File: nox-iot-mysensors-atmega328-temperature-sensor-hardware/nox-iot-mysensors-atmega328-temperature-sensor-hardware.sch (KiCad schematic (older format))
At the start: 14 parts, among them J1 Vin, J2 FTDI232, J3 AHT10, J4 TP4056, J5 Switch Connector, U1 ATmega328P-PU, U2 WAVGAT 3.3V, U3 NRF24L01+, Y1 16 MHZ

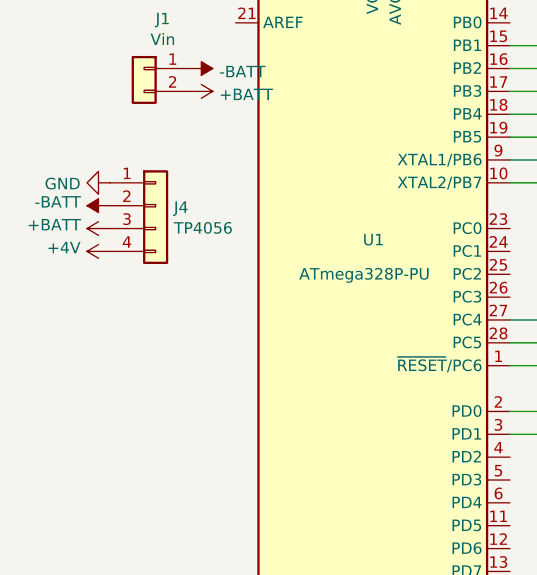
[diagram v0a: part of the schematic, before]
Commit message: updated with proper pcb
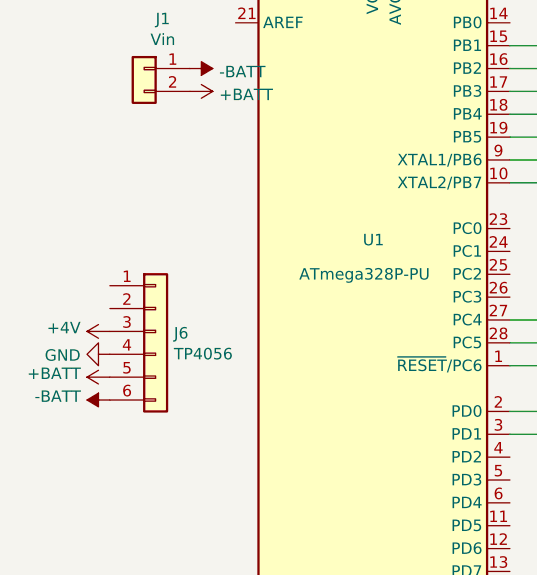
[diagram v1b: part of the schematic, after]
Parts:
- removed J4: TP4056, Connector_PinSocket_2.54mm:PinSocket_1x04_P2.54mm_Vertical, symbol Connector_Generic:Conn_01x04
- added J6: TP4056, Custom_Misc_Footprints:TP4056, symbol Connector_Generic:Conn_01x06
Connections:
- net +4V: now also J6.3 (Pin_3)
- net +BATT: now also J6.5 (Pin_5)
- net -BATT: now also J6.6 (Pin_6)
- net GND: now also J6.4 (Pin_4)
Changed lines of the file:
@@
 	6100 3750 6150 3750
-$Comp
-L Connector_Generic:Conn_01x04 J4
-U 1 1 5E764A8C
-P 2950 3350
-F 0 "J4" H 3030 3342 50  0000 L CNN
-F 1 "TP4056" H 3030 3251 50  0000 L CNN
-F 2 "Connector_PinSocket_2.54mm:PinSocket_1x04_P2.54mm_Vertical" H 2950 3350 50  0001 C CNN
-F 3 "~" H 2950 3350 50  0001 C CNN
-	1    2950 3350
-	1    0    0    -1
-$EndComp
-$Comp
-L power:GND #PWR09
-U 1 1 5E768EE0
-P 2750 3250
-F 0 "#PWR09" H 2750 3000 50  0001 C CNN
-F 1 "GND" V 2755 3122 50  0000 R CNN
-F 2 "" H 2750 3250 50  0001 C CNN
-F 3 "" H 2750 3250 50  0001 C CNN
-	1    2750 3250
-	0    1    1    0
-$EndComp
 $Comp
 L power:+4V #PWR0107
@@
 	1    9100 3400
 	-1   0    0    1
-$EndComp
-$Comp
-L power:+4V #PWR0108
-U 1 1 5E77B602
-P 2750 3550
-F 0 "#PWR0108" H 2750 3400 50  0001 C CNN
-F 1 "+4V" V 2765 3678 50  0000 L CNN
-F 2 "" H 2750 3550 50  0001 C CNN
-F 3 "" H 2750 3550 50  0001 C CNN
-	1    2750 3550
-	0    -1   -1   0
 $EndComp
 $Comp
@@
 $EndComp
 $Comp
-L power:+BATT #PWR0106
-U 1 1 5E78700E
-P 2750 3450
-F 0 "#PWR0106" H 2750 3300 50  0001 C CNN
-F 1 "+BATT" V 2765 3577 50  0000 L CNN
-F 2 "" H 2750 3450 50  0001 C CNN
-F 3 "" H 2750 3450 50  0001 C CNN
-	1    2750 3450
-	0    -1   -1   0
-$EndComp
-$Comp
 L power:-BATT #PWR0109
 U 1 1 5E787B63
@@
 	1    3100 2750
 	0    1    1    0
-$EndComp
-$Comp
-L power:-BATT #PWR0110
-U 1 1 5E788B81
-P 2750 3350
-F 0 "#PWR0110" H 2750 3200 50  0001 C CNN
-F 1 "-BATT" V 2765 3477 50  0000 L CNN
-F 2 "" H 2750 3350 50  0001 C CNN
-F 3 "" H 2750 3350 50  0001 C CNN
-	1    2750 3350
-	0    -1   -1   0
 $EndComp
 $Comp
@@
 	0    1    1    0
 $EndComp
+$Comp
+L Connector_Generic:Conn_01x06 J6
+U 1 1 5E78E301
+P 2950 3900
+F 0 "J6" H 3030 3892 50  0000 L CNN
+F 1 "TP4056" H 3030 3801 50  0000 L CNN
+F 2 "Custom_Misc_Footprints:TP4056" H 2950 3900 50  0001 C CNN
+F 3 "~" H 2950 3900 50  0001 C CNN
+	1    2950 3900
+	1    0    0    -1
+$EndComp
+$Comp
+L power:+4V #PWR0112
+U 1 1 5E79AF1E
+P 2750 3900
+F 0 "#PWR0112" H 2750 3750 50  0001 C CNN
+F 1 "+4V" V 2765 4028 50  0000 L CNN
+F 2 "" H 2750 3900 50  0001 C CNN
+F 3 "" H 2750 3900 50  0001 C CNN
+	1    2750 3900
+	0    -1   -1   0
+$EndComp
+$Comp
+L power:GND #PWR0114
+U 1 1 5E79B22C
+P 2750 4000
+F 0 "#PWR0114" H 2750 3750 50  0001 C CNN
+F 1 "GND" V 2755 3872 50  0000 R CNN
+F 2 "" H 2750 4000 50  0001 C CNN
+F 3 "" H 2750 4000 50  0001 C CNN
+	1    2750 4000
+	0    1    1    0
+$EndComp
+$Comp
+L power:+BATT #PWR0115
+U 1 1 5E79B58D
+P 2750 4100
+F 0 "#PWR0115" H 2750 3950 50  0001 C CNN
+F 1 "+BATT" V 2765 4227 50  0000 L CNN
+F 2 "" H 2750 4100 50  0001 C CNN
+F 3 "" H 2750 4100 50  0001 C CNN
+	1    2750 4100
+	0    -1   -1   0
+$EndComp
+$Comp
+L power:-BATT #PWR0116
+U 1 1 5E79B941
+P 2750 4200
+F 0 "#PWR0116" H 2750 4050 50  0001 C CNN
+F 1 "-BATT" V 2765 4327 50  0000 L CNN
+F 2 "" H 2750 4200 50  0001 C CNN
+F 3 "" H 2750 4200 50  0001 C CNN
+	1    2750 4200
+	0    -1   -1   0
+$EndComp
 $EndSCHEMATC
